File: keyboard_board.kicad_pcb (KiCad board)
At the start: 2 copper layers, 82.6 x 46.1 mm, 15 parts, among them J1 Conn_02x20_Odd_Even, J2 Trackpad Connector, J3 Rp500KB, J4 S3B-PH-SM4-TB, P1 S2B-PH-SM4-TB, P2 S2B-PH-SM4-TB, P3 S2B-PH-SM4-TB, P4 S2B-PH-SM4-TB, U1 SC0915, U2 74HC165, U3 74HC165

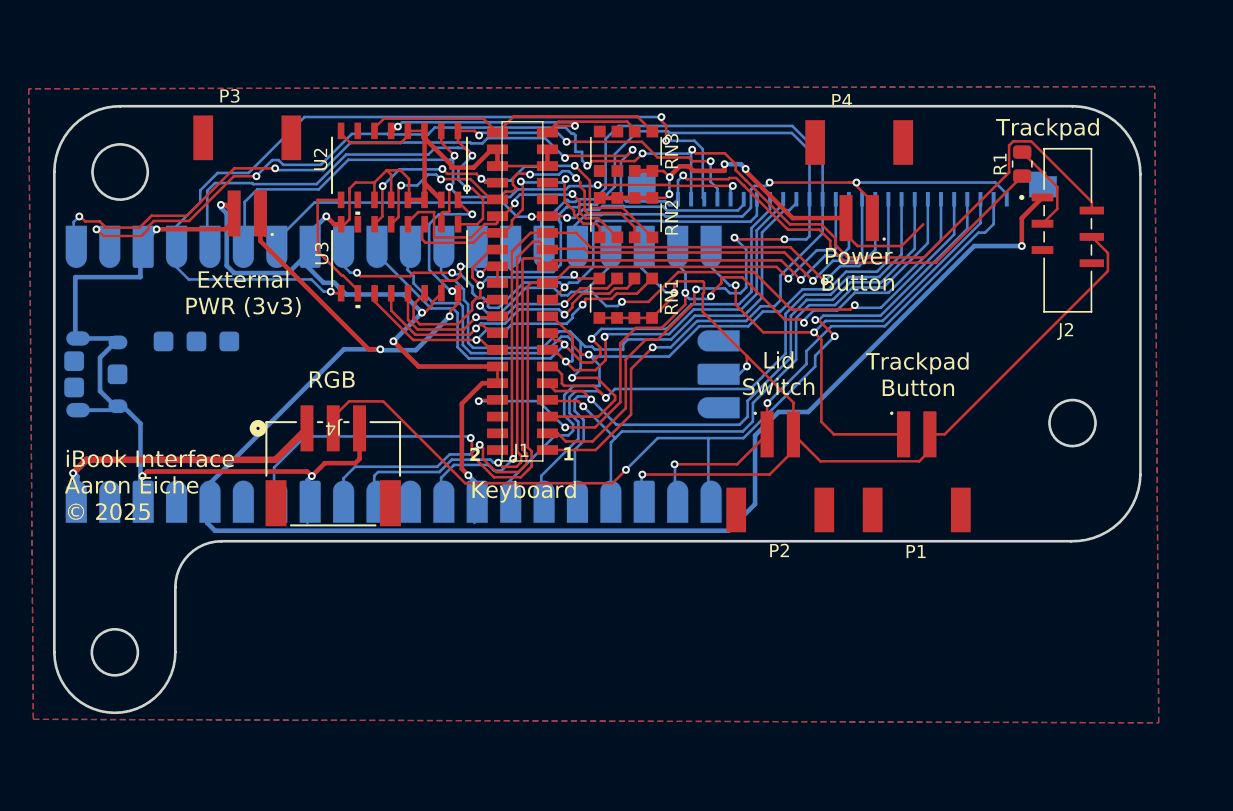
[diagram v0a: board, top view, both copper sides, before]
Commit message: Completes Pico version
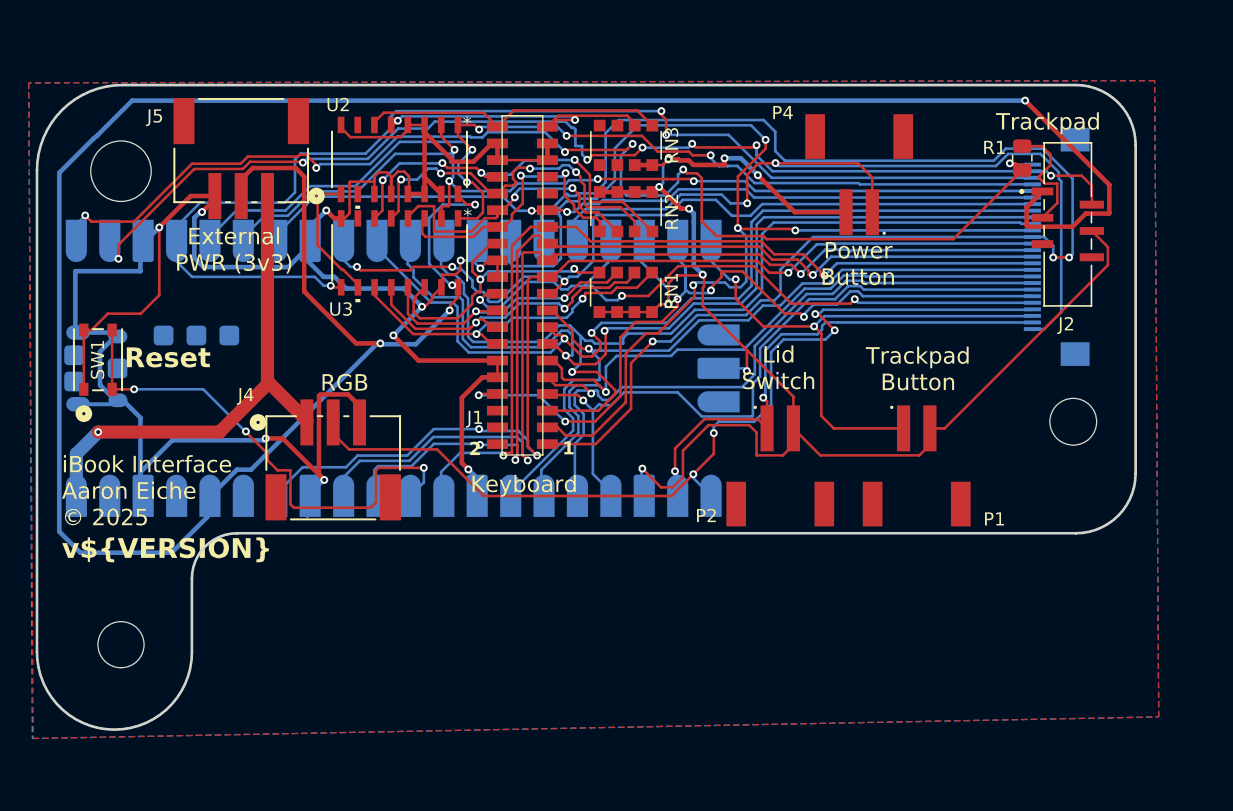
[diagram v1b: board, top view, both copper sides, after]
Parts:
- removed P3: S2B-PH-SM4-TB, Aaron:JST_S2B-PH-SM4-TB
- added J5: S3B-PH-SM4-TB, Aaron:CONN3_S3B-PH_JST, F.Cu at (194.1, 78.9)
- added SW1: Reset, Aaron:SW4_PTS815 SJM 250 SMTR LFS_CNK, F.Cu at (183.2, 94.8)
- J3: footprint Aaron:AMPHENOL_F52R-1A7H1-11026 -> Connector_FFC-FPC:Hirose_FH12-26S-0.5SH_1x26-1MP_P0.50mm_Horizontal
- moved J3 17.5 mm to (256.1, 86.2), turned to -90 degrees
- moved J1 0.45 mm to (215.5, 89.1)
- moved J2 0.45 mm to (257.0, 84.5)
- moved J4 0.45 mm to (201.1, 103.0)
- moved P1 0.45 mm to (245.5, 100.0)
- moved P2 0.45 mm to (235.1, 100.0)
- moved P4 0.45 mm to (241.1, 83.5)
- moved R1 0.45 mm to (253.5, 79.4)
- moved RN1 0.45 mm to (223.4, 89.6)
- moved RN2 0.45 mm to (223.4, 83.5)
- moved RN3 0.45 mm to (223.4, 78.4)
- moved U1 0.45 mm to (205.7, 95.4)
- moved U2 0.45 mm to (206.2, 79.5)
- moved U3 0.45 mm to (206.2, 86.6)
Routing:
- net +3.3V: track 136.3 -> 201.3 mm
- net Meta 1 (Fn): track 67.5 -> 108.3 mm, vias 1 -> 3
- net Net-(U1-~{RUN}): track 0.00 -> 39.0 mm, vias 0 -> 3
- net GND: track 297.1 -> 326.8 mm, vias 17 -> 19
- net PowerSwitch: track 41.1 -> 67.0 mm
- net Serial Out: track 66.3 -> 89.8 mm
- net Meta 29 (R Shift): track 38.9 -> 60.8 mm
- net Meta 19 (R Option): track 44.0 -> 64.8 mm
- net Shift Clock: track 52.6 -> 73.0 mm
- net Paralell Latch: track 60.4 -> 80.3 mm
- net Meta 15 (L Shift): track 48.1 -> 67.1 mm
- net Meta 13 (Ctrl): track 50.0 -> 67.9 mm
- net VBUS: track 21.5 -> 38.7 mm
- net Meta 5 (Command): track 55.5 -> 72.0 mm
- net Meta 3 (Option): track 73.5 -> 88.0 mm, vias 3 -> 4
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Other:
- board size 82.6 x 46.1 mm -> 83.5 x 49 mm
- board text added: "*"
- board text added: "Reset"
- board text added: "v${VERSION}"

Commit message: Updates to Pico version
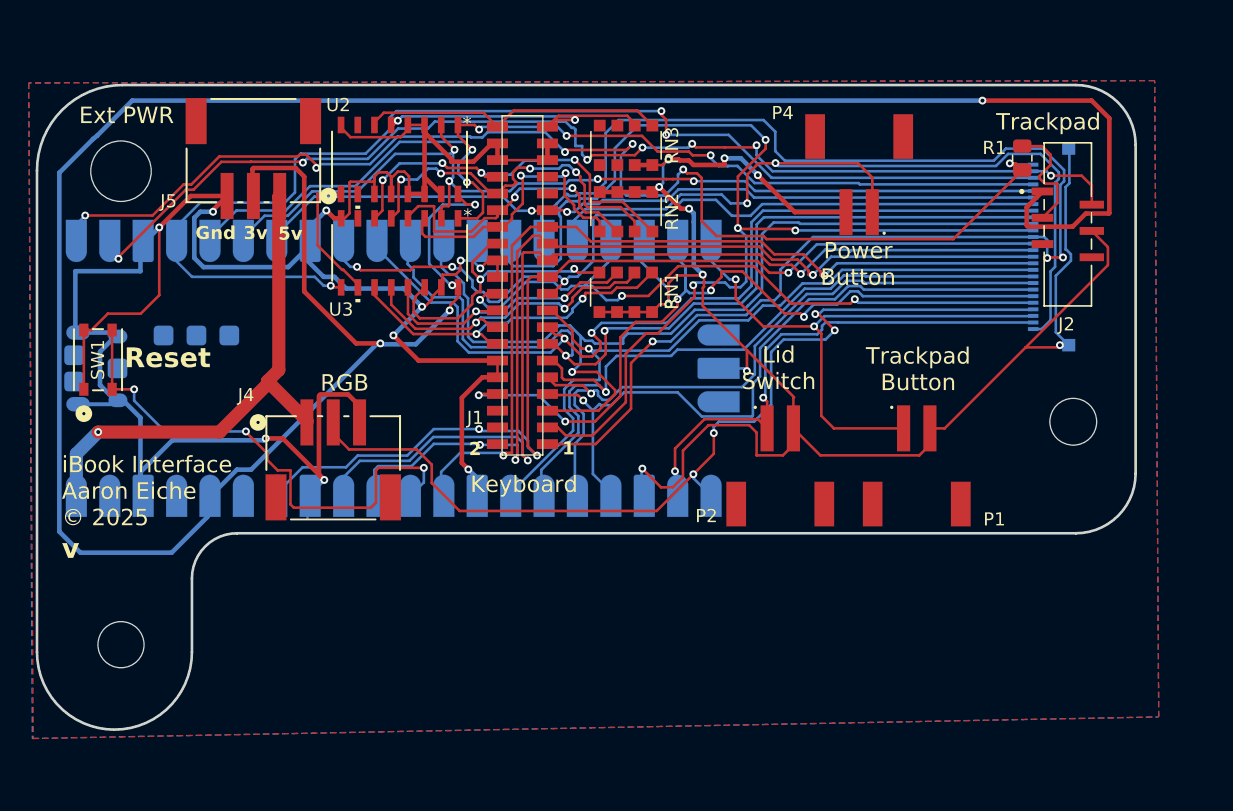
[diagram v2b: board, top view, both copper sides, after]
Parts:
- J3: footprint Connector_FFC-FPC:Hirose_FH12-26S-0.5SH_1x26-1MP_P0.50mm_Horizontal -> Aaron:AMPHENOL_10051922-2610ELF
- moved J5 0.93 mm to (195.1, 78.9)
- moved J3 0.06 mm to (256.2, 86.2)
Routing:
- net GND: track 326.8 -> 348.2 mm, vias 19 -> 20
- net RGB: track 70.6 -> 72.3 mm
- net +3.3V: track 201.3 -> 202.3 mm
- net TP_RX: track 87.0 -> 86.5 mm
- net Net-(U1-~{RUN}): track 39.0 -> 39.5 mm
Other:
- board text added: "3v"
- board text added: "5v"
- board text added: "Ext PWR"
- board text added: "Gnd"
- board text added: "v${REVISION}"
- board text removed: "External PWR (3v3)"
- board text removed: "v${VERSION}"

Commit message: Reworks Pico-based into discrete components
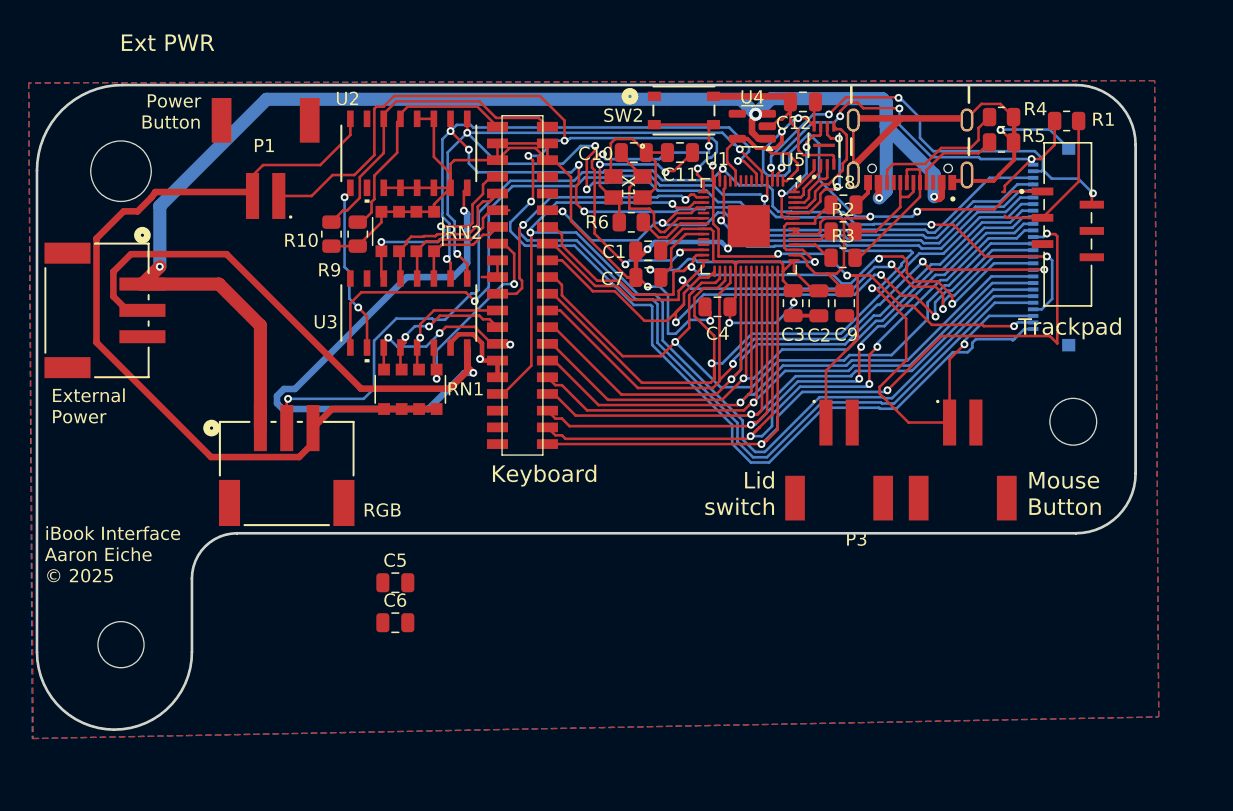
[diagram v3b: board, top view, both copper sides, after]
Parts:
- removed P4: S2B-PH-SM4-TB, Aaron:JST_S2B-PH-SM4-TB
- removed RN3: 10K, Resistor_SMD:R_Array_Convex_4x1206
- removed SW1: Reset, Aaron:SW4_PTS815 SJM 250 SMTR LFS_CNK
- added C1: 0.1uF, Capacitor_SMD:C_0805_2012Metric, F.Cu at (225.1, 86.5)
- added C10: 15pF, Capacitor_SMD:C_0805_2012Metric, F.Cu at (224.0, 79.0)
- added C11: 15pF, Capacitor_SMD:C_0805_2012Metric, F.Cu at (227.5, 79.0)
- added C12: 0.1uF, Capacitor_SMD:C_0805_2012Metric, F.Cu at (236.8, 75.2)
- added C2: 0.1uF, Capacitor_SMD:C_0805_2012Metric, F.Cu at (238.1, 90.5)
- added C3: 0.1uF, Capacitor_SMD:C_0805_2012Metric, F.Cu at (236.1, 90.5)
- added C4: 0.1uF, Capacitor_SMD:C_0805_2012Metric, F.Cu at (230.4, 90.7)
- added C5: 0.1uF, Capacitor_SMD:C_0805_2012Metric, F.Cu at (205.9, 111.7)
- added C6: 0.1uF, Capacitor_SMD:C_0805_2012Metric, F.Cu at (205.9, 114.7)
- added C7: 0.1uF, Capacitor_SMD:C_0805_2012Metric, F.Cu at (225.1, 88.5)
- added C8: 0.1uF, Capacitor_SMD:C_0805_2012Metric, F.Cu at (239.9, 83.0)
- added C9: 0.1uF, Capacitor_SMD:C_0805_2012Metric, F.Cu at (240.0, 90.5)
- added J6: USB4105-GF-A, Aaron:GCT_USB4105-GF-A, F.Cu at (245.0, 76.5)
- added P3: Lid Switch, Aaron:JST_S2B-PH-SM4-TB, F.Cu at (239.6, 99.5)
- added R10: 10K, Resistor_SMD:R_0805_2012Metric, F.Cu at (201.0, 85.2)
- added R2: 27, Resistor_SMD:R_0805_2012Metric, F.Cu at (239.9, 85.0)
- added R3: 27, Resistor_SMD:R_0805_2012Metric, F.Cu at (239.9, 87.0)
- added R4: 5k1, Resistor_SMD:R_0805_2012Metric, F.Cu at (251.9, 76.3)
- added R5: 5k1, Resistor_SMD:R_0805_2012Metric, F.Cu at (251.9, 78.2)
- added R6: 1K, Resistor_SMD:R_0805_2012Metric, F.Cu at (223.8, 84.3)
- added R9: 10K, Resistor_SMD:R_0805_2012Metric, F.Cu at (203.0, 85.2)
- added SW2: Reset, Aaron:SW4_PTS815 SJM 250 SMTR LFS_CNK, F.Cu at (227.8, 75.8)
- added U4: AP2112K-3.3, Package_TO_SOT_SMD:SOT-23-5, F.Cu at (233.0, 77.0)
- added U5: W25Q16JVSS, Aaron:USON-8_UX_2x3x0p6_WIN, F.Cu at (238.4, 78.5)
- added X1: ABM8-272-T3, Aaron:ABM8-272-T3_ABR, F.Cu at (223.6, 81.6)
- J4: value S3B-PH-SM4-TB -> RGB Out
- J5: value S3B-PH-SM4-TB -> Alt Power Input
- P1: value S2B-PH-SM4-TB -> Power Button
- P2: value S2B-PH-SM4-TB -> Mouse Button
- U1: value SC0915 -> RP2040; footprint SC0915:MODULE_SC0915 -> Package_DFN_QFN:QFN-56-1EP_7x7mm_P0.4mm_EP3.2x3.2mm; moved to F.Cu
- moved P1 52.6 mm to (196.0, 82.3), turned to 0 degrees
- moved U1 29.1 mm to (232.7, 84.6)
- moved RN1 18.0 mm to (207.0, 97.0)
- moved J5 17.0 mm to (183.2, 91.0), turned to 90 degrees
- moved RN2 16.7 mm to (206.8, 85.0)
- moved P2 13.9 mm to (249.0, 99.5)
- moved U3 4.63 mm to (206.9, 91.2)
- moved R1 4.40 mm to (256.9, 76.6), turned to 0 degrees
- moved J4 3.56 mm to (197.6, 103.4)
- moved U2 0.85 mm to (206.9, 79.1)
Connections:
- J4 pad 1: VBUS -> USB_VBUS
- J5 pad 1: VBUS -> USB_VBUS
- P1 pad 1: MouseButton  -> PowerSwitch
- P2 pad 1: LidSwitch -> MouseButton 
- RN1 pad 5: Col 14 -> Col 26
- RN1 pad 6: Col 16 -> Col 18
- RN1 pad 7: Col 18 -> Col 16
- RN1 pad 8: Col 26 -> Col 14
- RN2 pad 5: Col 28 -> Col 34
- RN2 pad 6: Col 30 -> Col 32
- RN2 pad 7: Col 32 -> Col 30
- RN2 pad 8: Col 34 -> Col 28
- U1 pad 1: TP_TX -> +3.3V
- U1 pad 10: Meta 15 (L Shift) -> +3.3V
- U1 pad 11: Meta 13 (Ctrl) -> unconnected-(U1-GPIO8-Pad11)
- U1 pad 12: Meta 5 (Command) -> MouseButton 
- U1 pad 13: GND -> RGB
- U1 pad 14: Meta 3 (Option) -> LidSwitch
- U1 pad 15: Meta 1 (Fn) -> PowerSwitch
- U1 pad 16: PowerSwitch -> Power LED V+
- U1 pad 17: Power LED V+ -> Caps LED V+
- U1 pad 18: GND -> Meta 29 (R Shift)
- U1 pad 19: Caps LED V+ -> Net-(JP1-B)
- U1 pad 2: TP_RX -> TP_TX
- U1 pad 20: MouseButton  -> Xin
- U1 pad 21: RGB -> Xout
- U1 pad 22: LidSwitch -> +3.3V
- U1 pad 23: GND -> +1V1
- U1 pad 24: Row 7 -> SWCLK
- U1 pad 25: Row 9 -> SWD
- U1 pad 26: Row 11 -> RESET
- U1 pad 27: Row 17 -> Row 27
- U1 pad 28: GND -> Row 25
- U1 pad 29: Row 27 -> Row 23
- U1 pad 3: GND -> TP_RX
- U1 pad 30: Net-(U1-~{RUN}) -> Row 21
- U1 pad 31: Row 25 -> Meta 19 (R Option)
- U1 pad 32: Row 23 -> Row 17
- U1 pad 33: GND -> +3.3V
- U1 pad 34: Row 21 -> Meta 15 (L Shift)
- U1 pad 35: unconnected-(U1-ADC_VREF-Pad35) -> Meta 13 (Ctrl)
- U1 pad 36: +3.3V -> Row 11
- U1 pad 37: unconnected-(U1-3V3_EN-Pad37) -> Row 9
- U1 pad 38: GND -> Row 7
- U1 pad 39: VSYS -> Meta 5 (Command)
- U1 pad 40: VBUS -> Meta 3 (Option)
- U1 pad 7: Meta 29 (R Shift) -> unconnected-(U1-GPIO5-Pad7)
- U1 pad 8: GND -> unconnected-(U1-GPIO6-Pad8)
- U1 pad 9: Meta 19 (R Option) -> unconnected-(U1-GPIO7-Pad9)
- U2 pad 5: Col 39 -> Col 40
- U2 pad 6: Col 40 -> Col 39
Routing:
- net GND: track 348.2 -> 223.9 mm, vias 20 -> 6
- net USB_VBUS: track 0.00 -> 108.8 mm, vias 0 -> 4
- net TP_TX: track 93.4 -> 33.6 mm, vias 6 -> 4
- net TP_RX: track 86.5 -> 34.3 mm, vias 7 -> 4
- net PowerSwitch: track 66.7 -> 109.8 mm, vias 2 -> 4
- net Meta 1 (Fn): track 108.0 -> 67.3 mm
- net Net-(U1-~{RUN}): track 39.5 -> 0.00 mm, vias 3 -> 0
- net VBUS: track 39.1 -> 0.00 mm, vias 1 -> 0
- net RESET: track 0.00 -> 31.6 mm, vias 0 -> 4
- net +1V1: track 0.00 -> 28.1 mm, vias 0 -> 2
- net Meta 3 (Option): track 88.0 -> 60.0 mm, vias 4 -> 3
- net Row 25: track 72.5 -> 47.7 mm
- net Power LED V+: track 52.0 -> 76.4 mm, vias 3 -> 2
- net Row 21: track 77.1 -> 54.4 mm, vias 3 -> 1
- net Row 23: track 73.5 -> 51.0 mm, vias 2 -> 3
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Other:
- board text added: "External Power"
- board text added: "Lid switch"
- board text added: "Mouse Button"
- board text removed: "*"
- board text removed: "1"
- board text removed: "2"
- board text removed: "3v"
- board text removed: "5v"
- board text removed: "Gnd"
- board text removed: "Lid Switch"
- board text removed: "Reset"
- board text removed: "Trackpad Button"
- board text removed: "v${REVISION}"

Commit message: prod version, I think
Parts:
- added C13: 1uF, Capacitor_SMD:C_0603_1608Metric, F.Cu at (230.7, 95.2)
- added C14: 10uF, Capacitor_SMD:C_0805_2012Metric, F.Cu at (239.1, 84.5)
- added C15: 10uF, Capacitor_SMD:C_0805_2012Metric, F.Cu at (243.8, 87.5)
- added J7: Power, Connector_PinHeader_2.54mm:PinHeader_1x03_P2.54mm_Vertical, F.Cu at (226.4, 105.2)
- added JP1: Jumper_2_Small_Open, Jumper:SolderJumper-2_P1.3mm_Open_RoundedPad1.0x1.5mm, F.Cu at (199.1, 76.2)
- added R7: 1K, Resistor_SMD:R_0603_1608Metric, F.Cu at (238.3, 93.4)
- added R8: 10K, Resistor_SMD:R_0603_1608Metric, F.Cu at (237.9, 97.8)
- added SW1: Boot Select, Aaron:SW4_PTS815 SJM 250 SMTR LFS_CNK, F.Cu at (247.2, 93.2)
- C1, C10, C11, C12, C2, C3, C4, C5, C6, C7, C8: footprint Capacitor_SMD:C_0805_2012Metric -> Capacitor_SMD:C_0603_1608Metric
- C9: value 0.1uF -> 1uF; footprint Capacitor_SMD:C_0805_2012Metric -> Capacitor_SMD:C_0603_1608Metric
- J3: value Rp500KB -> Conn_01x03_Pin; footprint Aaron:AMPHENOL_10051922-2610ELF -> Connector_PinHeader_2.54mm:PinHeader_1x03_P2.54mm_Vertical; moved to F.Cu
- J5: value Alt Power Input -> Conn_01x04_Pin; footprint Aaron:CONN3_S3B-PH_JST -> Connector_PinHeader_2.54mm:PinHeader_1x04_P2.54mm_Vertical
- R2, R3, R4, R5, R6: footprint Resistor_SMD:R_0805_2012Metric -> Resistor_SMD:R_0603_1608Metric
- U4: value AP2112K-3.3 -> XC6220B331MR
- moved J3 67.2 mm to (189.8, 76.2), turned to 90 degrees
- moved P2 62.2 mm to (186.8, 101.3), turned to 90 degrees
- moved P3 53.3 mm to (186.8, 92.2), turned to 90 degrees
- moved J4 47.4 mm to (245.0, 103.2)
- moved C5 40.1 mm to (238.7, 88.6), turned to -90 degrees
- moved C6 39.9 mm to (238.6, 91.9)
- moved P1 31.9 mm to (227.9, 82.1)
- moved C12 22.7 mm to (234.9, 97.8)
- moved SW2 22.0 mm to (247.3, 86.0), turned to 90 degrees
- moved J5 20.8 mm to (198.4, 105.2)
- moved U5 17.3 mm to (237.5, 95.8), turned to 180 degrees
- moved C10 15.3 mm to (239.1, 81.5), turned to -90 degrees
- moved R2 15.2 mm to (232.4, 98.2), turned to -90 degrees
- moved R3 14.4 mm to (230.9, 98.2), turned to -90 degrees
- moved R4 13.0 mm to (239.1, 78.5), turned to -90 degrees
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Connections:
- J5 pad 1: USB_VBUS -> IO5
- J5 pad 2: +3.3V -> IO6
- J5 pad 3: GND -> IO7
- J5 pad 4: (no net) -> IO8
- SW2 pad 1: GND -> RESET
- SW2 pad 2: RESET -> GND
- U1 pad 11: unconnected-(U1-GPIO8-Pad11) -> IO8
- U1 pad 7: unconnected-(U1-GPIO5-Pad7) -> IO5
- U1 pad 8: unconnected-(U1-GPIO6-Pad8) -> IO6
- U1 pad 9: unconnected-(U1-GPIO7-Pad9) -> IO7
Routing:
- net PowerSwitch: track 109.8 -> 9.11 mm, vias 4 -> 2
- net GND: track 223.9 -> 286.3 mm, vias 6 -> 53
- net RGB: track 83.2 -> 29.9 mm, vias 4 -> 2
- net IO6: track 0.00 -> 52.5 mm, vias 0 -> 1
- net IO7: track 0.00 -> 52.4 mm, vias 0 -> 1
- net IO8: track 0.00 -> 52.0 mm, vias 0 -> 1
- net Meta 1 (Fn): track 67.3 -> 18.4 mm, vias 3 -> 0
- net IO5: track 0.00 -> 47.5 mm, vias 0 -> 1
- net SWD: track 0.00 -> 47.4 mm, vias 0 -> 1
- net Shift Clock: track 93.1 -> 48.2 mm, vias 6 -> 3
- net Meta 19 (R Option): track 56.8 -> 13.3 mm, vias 1 -> 0
- net SWCLK: track 0.00 -> 42.9 mm, vias 0 -> 1
- net Meta 3 (Option): track 60.0 -> 17.6 mm, vias 3 -> 0
- net Net-(JP1-B): track 0.00 -> 42.4 mm, vias 0 -> 2
- net Paralell Latch: track 90.6 -> 48.8 mm, vias 5 -> 3
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- added copper zone on In1.Cu, net GND
- added copper zone on In2.Cu, net GND
- added copper zone on F.Cu, net USB_VBUS
- removed copper zone on F.Cu, net GND
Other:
- outline, holes or cut-outs redrawn
- copper layers 2 -> 4
- board text added: "3v3"
- board text added: "5"
- board text added: "5v"
- board text added: "6"
- board text added: "7"
- board text added: "8"
- board text added: "BOOTSEL"
- board text added: "Debug"
- board text added: "ENABLE"
- board text added: "GND"
- board text added: "GPIO"
- board text added: "Gnd"
- board text added: "JLCJLCJLCJLC"
- board text added: "RESET"
- board text added: "SWCLK"
- board text added: "SWDIO"
- board text added: "iBook Interface Aaron Eiche"
- board text added: "v${VERSION}"
- board text removed: "Ext PWR"
- board text removed: "External Power"
- board text removed: "iBook Interface Aaron Eiche © 2025"
